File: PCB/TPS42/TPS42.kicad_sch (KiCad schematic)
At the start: 80 parts, among them J1 PJ-320A, J11 Conn_01x06, J13 Conn_01x09, J14 FH12-10S-0.5SH, J2 Conn_01x09, J3 TP Sensor Module, J4 TP Module, J5 Conn_01x02, J6 OLED, J7 TrackPoint, J8 Battery, J9 TP Sensor Module, SW1 SW_DPST_x2, SW2 Reset, SW3 Reset, U1 ProMicro, U11 Hole, U12 Hole, U14 ProMicro, U2 Hole, U3 Hole, U4 Hole, U5 Hole, U7 Hole, U8 Hole, U9 Hole

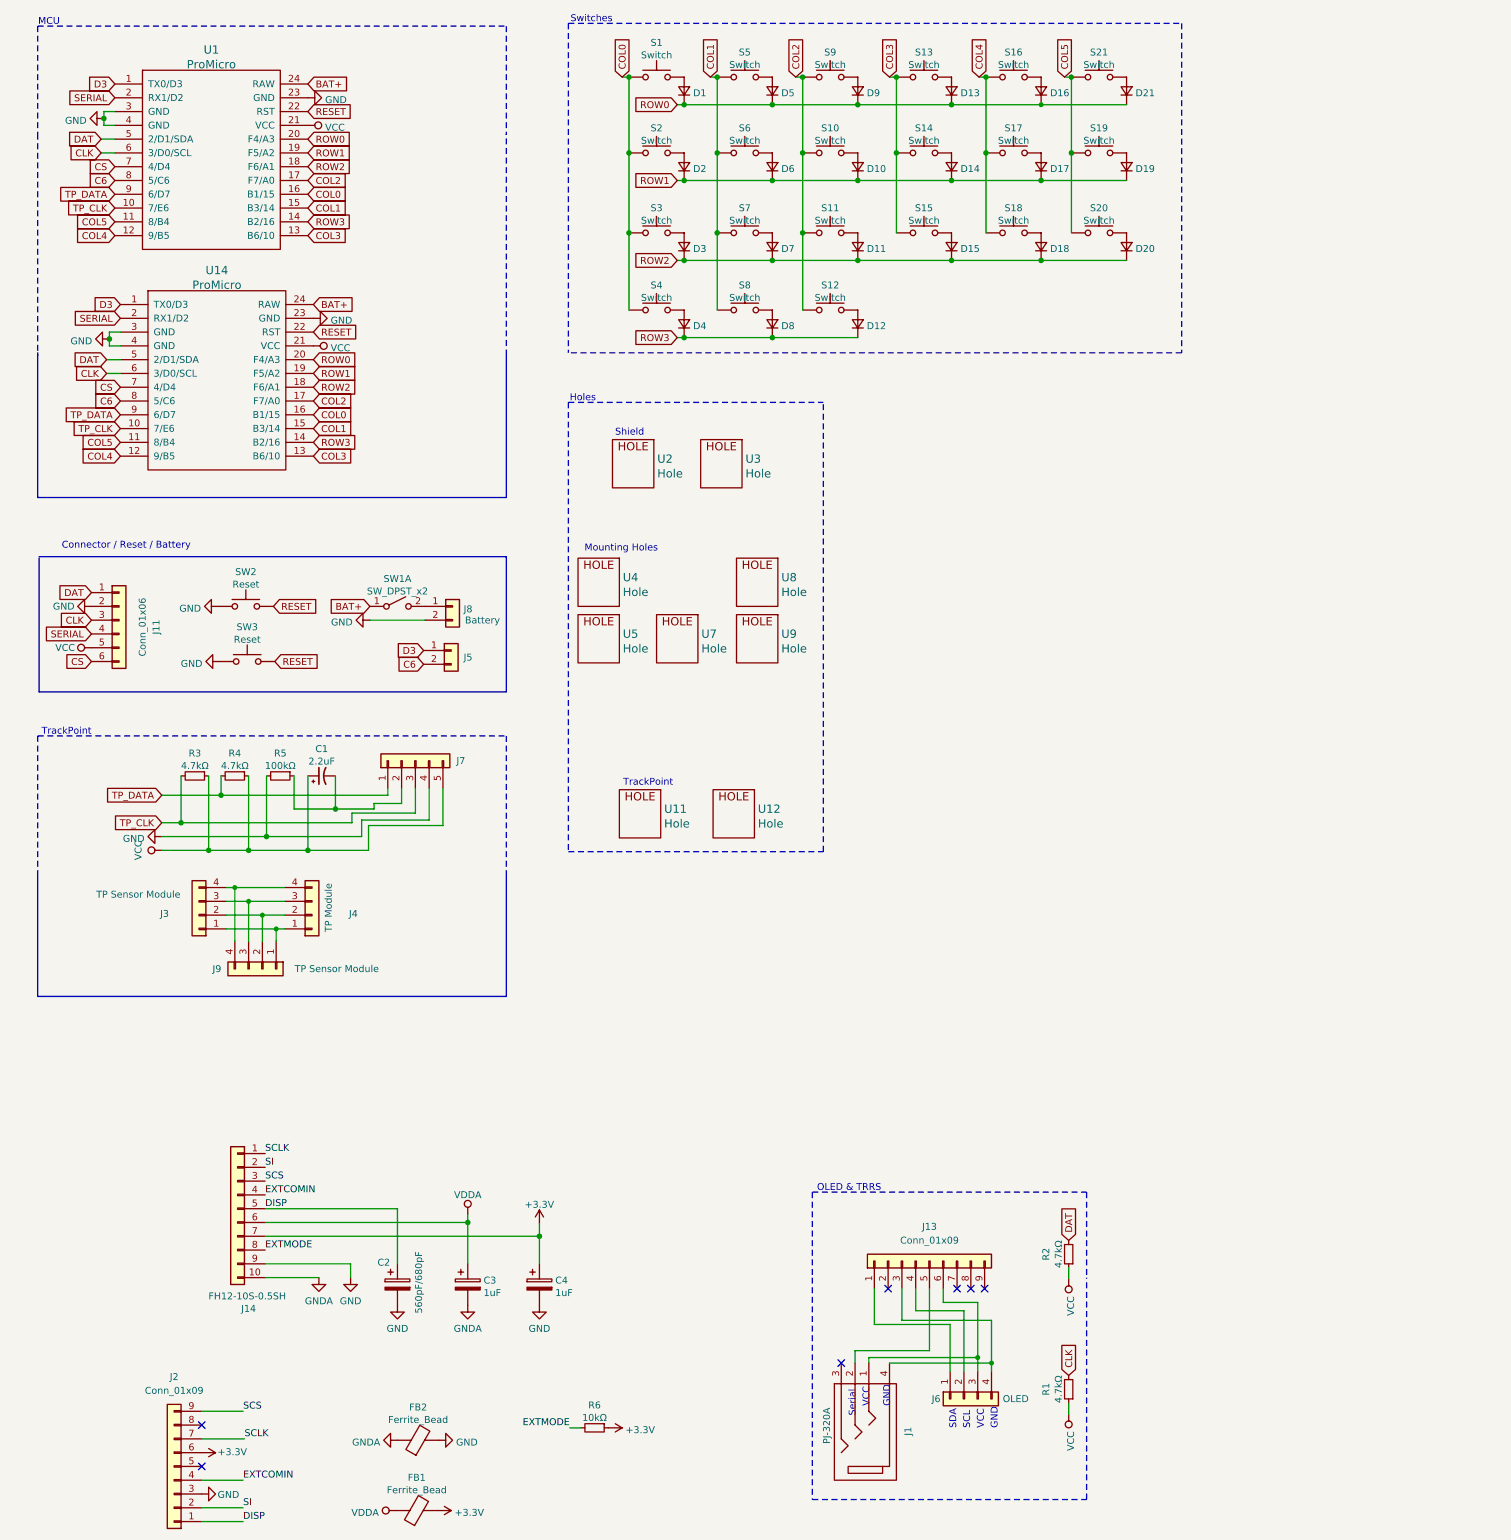
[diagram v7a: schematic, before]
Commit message: Added oled/trrs shield
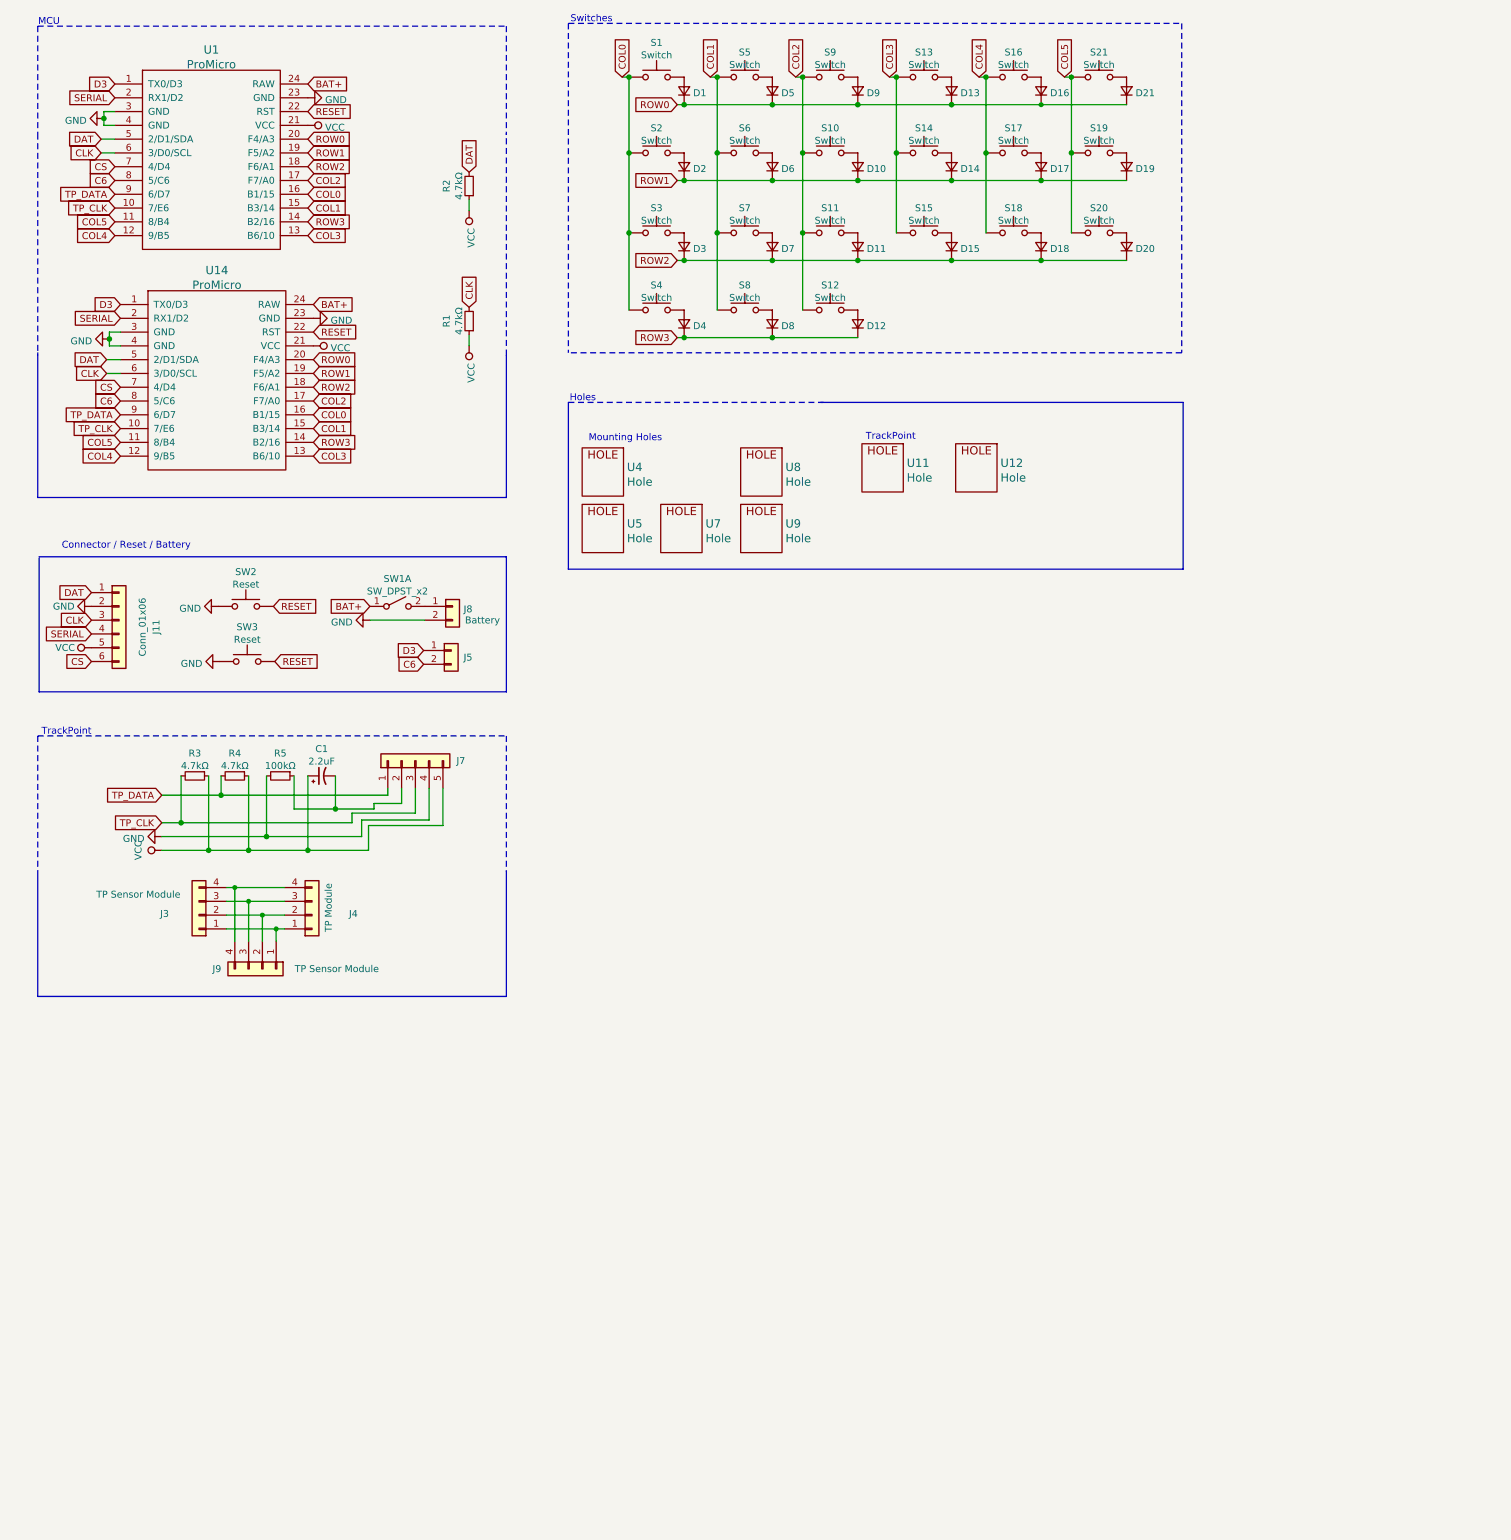
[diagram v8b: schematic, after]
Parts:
- removed C2: 560pF/680pF, TPS42:C_0603_1608Metric_Pad1.08x0.95mm_HandSolder_Reversable, symbol Device:CP
- removed C3, C4: 1uF, TPS42:C_0603_1608Metric_Pad1.08x0.95mm_HandSolder_Reversable, symbol Device:CP
- removed FB1, FB2: Ferrite_Bead, Resistor_SMD:R_0805_2012Metric_Pad1.20x1.40mm_HandSolder, symbol Device:Ferrite_Bead
- removed J1: PJ-320A, TPS42:MJ-4PP-9, symbol TPS42:MJ-4PP-9
- removed J13, J2: Conn_01x09, TPS42:Connector_Reversable_3x3, symbol Connector_Generic:Conn_01x09
- removed J14: FH12-10S-0.5SH, Connector_FFC-FPC:Hirose_FH12-10S-0.5SH_1x10-1MP_P0.50mm_Horizontal, symbol Connector_Generic:Conn_01x10
- removed J6: OLED, TPS42:OLED, symbol Connector_Generic:Conn_01x04
- removed R6: 10kΩ, TPS42:R_0603_1608Metric_Pad0.98x0.95mm_HandSolder_Reversable, symbol Device:R_Small
- removed U2, U3: Hole, TPS42:M2_HOLE_PCB, symbol TPS42:Hole
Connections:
- no-connect marks 7 -> 0
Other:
- note removed: "GND"
- note removed: "OLED & TRRS"
- note removed: "SCL"
- note removed: "SDA"
- note removed: "Serial"
- note removed: "Shield"
- note removed: "VCC"
- moved on the sheet: R1, R2, U11, U12, U4, U5, U7, U8, U9
